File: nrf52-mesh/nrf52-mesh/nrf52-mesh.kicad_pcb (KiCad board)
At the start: 2 copper layers, 57.9 x 56.6 mm, 27 parts, among them J1 Conn_01x20_Male, J2 Conn_01x04_Male, J3 Conn_01x06_Male, U1 BL652

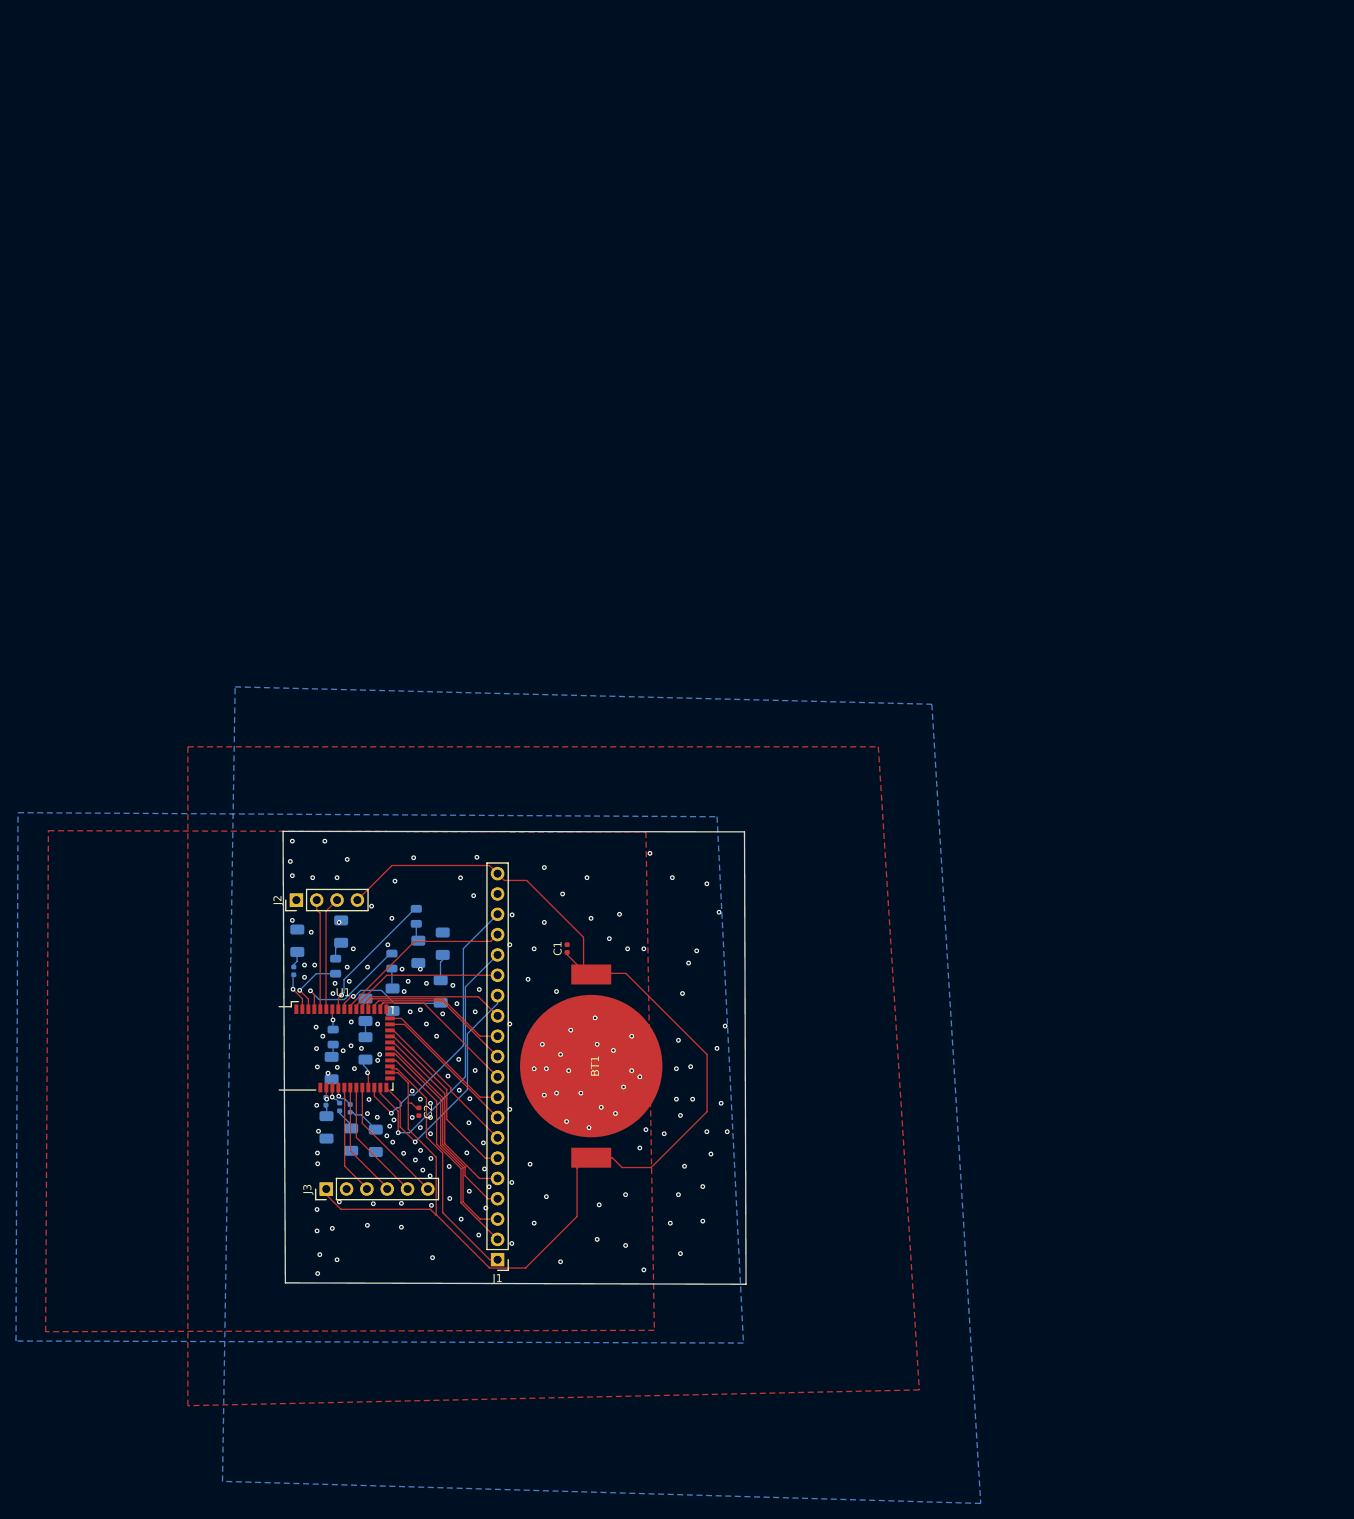
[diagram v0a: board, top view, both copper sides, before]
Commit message: CP2102N + MAX1555 + FAN5341 + TPS560200 + TLV62568
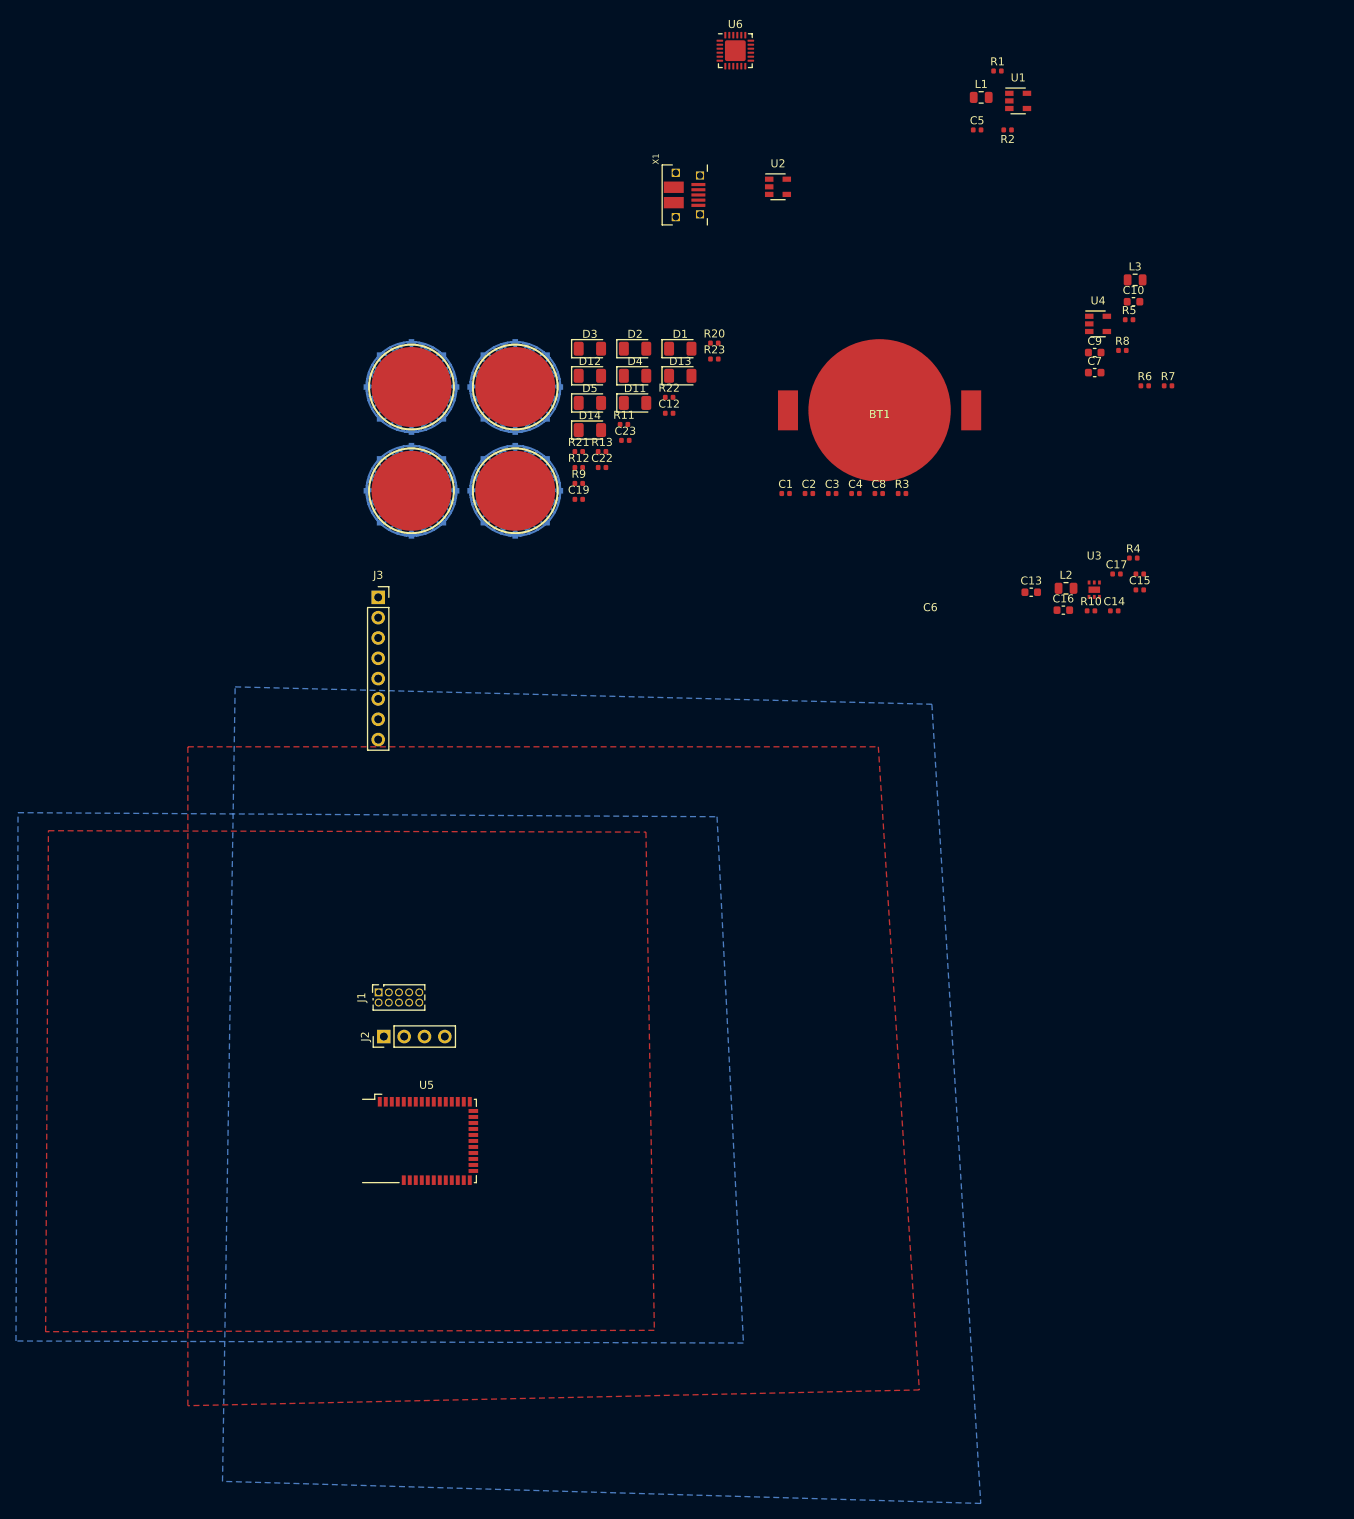
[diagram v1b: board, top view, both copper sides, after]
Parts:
- removed D10, D6, D7, D8, D9: LED, LED_SMD:LED_1206_3216Metric
- added C10: 10uF, Capacitor_SMD:C_0603_1608Metric, F.Cu at (288.0, -14.1)
- added C11: Cap, kifootp:CAPBUTTON, F.Cu at (197.8, -3.42)
- added C12: 100pF, Capacitor_SMD:C_0402_1005Metric, F.Cu at (230.0, -0.14)
- added C13: 10uF, Capacitor_SMD:C_0603_1608Metric, F.Cu at (275.2, 22.2)
- added C14: 1uF, Capacitor_SMD:C_0402_1005Metric, F.Cu at (285.6, 24.6)
- added C15: 1uF, Capacitor_SMD:C_0402_1005Metric, F.Cu at (288.8, 21.9)
- added C16: 10uF, Capacitor_SMD:C_0603_1608Metric, F.Cu at (279.3, 24.5)
- added C17: 0.1uF, Capacitor_SMD:C_0402_1005Metric, F.Cu at (285.9, 19.9)
- added C18: Cap, kifootp:CAPBUTTON, F.Cu at (210.7, 9.55)
- added C19: 100pF, Capacitor_SMD:C_0402_1005Metric, F.Cu at (218.7, 10.6)
- added C20: Cap, kifootp:CAPBUTTON, F.Cu at (210.7, -3.42)
- added C21: Cap, kifootp:CAPBUTTON, F.Cu at (197.8, 9.55)
- added C22: 100pF, Capacitor_SMD:C_0402_1005Metric, F.Cu at (221.6, 6.64)
- added C23: 100pF, Capacitor_SMD:C_0402_1005Metric, F.Cu at (224.5, 3.25)
- added C3: 0.1uF, Capacitor_SMD:C_0402_1005Metric, F.Cu at (250.4, 9.89)
- added C4: 1uF, Capacitor_SMD:C_0402_1005Metric, F.Cu at (253.3, 9.89)
- added C5: 4.7uF, Capacitor_SMD:C_0402_1005Metric, F.Cu at (268.5, -35.6)
- added C6: 10uF, Capacitor_SMD:C_0402_1005Metric, F.Cu at (288.8, 19.9)
- added C7: 10uF, Capacitor_SMD:C_0603_1608Metric, F.Cu at (283.2, -5.22)
- added C8: 0.1uF, Capacitor_SMD:C_0402_1005Metric, F.Cu at (256.2, 9.89)
- added C9: 10uF, Capacitor_SMD:C_0603_1608Metric, F.Cu at (283.2, -7.73)
- added D11: LED, LED_SMD:LED_1206_3216Metric, F.Cu at (225.7, -1.43)
- added D12: LED, LED_SMD:LED_1206_3216Metric, F.Cu at (220.1, -4.82)
- added D13: LED, LED_SMD:LED_1206_3216Metric, F.Cu at (231.4, -4.82)
- added D14: LED, LED_SMD:LED_1206_3216Metric, F.Cu at (220.1, 1.96)
- added L1: 2.2uH, Inductor_SMD:L_0805_2012Metric, F.Cu at (269.0, -39.6)
- added L2: 10uH, Inductor_SMD:L_0805_2012Metric, F.Cu at (279.6, 21.7)
- added L3: 10uH, Inductor_SMD:L_0805_2012Metric, F.Cu at (288.2, -16.8)
- added R11: 10kOhm, Resistor_SMD:R_0402_1005Metric, F.Cu at (224.3, 1.26)
- added R12: 10kOhm, Resistor_SMD:R_0402_1005Metric, F.Cu at (218.7, 6.64)
- added R13: 10kOhm, Resistor_SMD:R_0402_1005Metric, F.Cu at (221.6, 4.65)
- added R20: 10kOhm, Resistor_SMD:R_0402_1005Metric, F.Cu at (235.6, -8.91)
- added R21: 10kOhm, Resistor_SMD:R_0402_1005Metric, F.Cu at (218.7, 4.65)
- added R22: 10kOhm, Resistor_SMD:R_0402_1005Metric, F.Cu at (230.0, -2.13)
- added R23: 10kOhm, Resistor_SMD:R_0402_1005Metric, F.Cu at (235.6, -6.92)
- added U2: MAX1555, Package_TO_SOT_SMD:SOT-23-5, F.Cu at (243.6, -28.4)
- added U3: FAN5341, kifootp:FAN5341, F.Cu at (283.1, 21.9)
- added U4: TPS560200, Package_TO_SOT_SMD:SOT-23-5, F.Cu at (283.6, -11.3)
- added U5: BL652, RF_Module:Laird_BL652, F.Cu at (199.7, 90.8)
- added U6: CP2102N-A01-GQFN24, Package_DFN_QFN:QFN-24-1EP_4x4mm_P0.5mm_EP2.6x2.6mm, F.Cu at (238.3, -45.5)
- added X1: USBFCI_10103594, kifootp:FCI_10103594_MILL, F.Cu at (229.1, -27.4)
- C1: value 4.7uF -> 1uF
- C2: value 0.1uF -> 4.7uF
- D1, D2, D3, D4, D5: moved to F.Cu
- J1: value Conn_01x20_Male -> Conn_02x05_Odd_Even; footprint Connector_PinHeader_2.54mm:PinHeader_1x20_P2.54mm_Vertical -> Connector_PinSocket_1.27mm:PinSocket_2x05_P1.27mm_Vertical
- J3: value Conn_01x06_Male -> Conn_01x08; footprint Connector_PinHeader_2.54mm:PinHeader_1x06_P2.54mm_Vertical -> Connector_PinSocket_2.54mm:PinSocket_1x08_P2.54mm_Vertical
- R1: value R -> 450kOhm; moved to F.Cu
- R10: value R -> 1kOhm; footprint Resistor_SMD:R_1206_3216Metric -> Resistor_SMD:R_0402_1005Metric; moved to F.Cu
- R2, R3: value R -> 100kOhm; moved to F.Cu
- R4: value R -> 20 Ohm; moved to F.Cu
- R5: value R -> 200kOhm; footprint Resistor_SMD:R_0805_2012Metric -> Resistor_SMD:R_0402_1005Metric; moved to F.Cu
- R6: value R -> 100kOhm; footprint Resistor_SMD:R_0805_2012Metric -> Resistor_SMD:R_0402_1005Metric; moved to F.Cu
- R7: value R -> 105kOhm; footprint Resistor_SMD:R_0805_2012Metric -> Resistor_SMD:R_0402_1005Metric; moved to F.Cu
- R8: value R -> 20kOhm; footprint Resistor_SMD:R_0805_2012Metric -> Resistor_SMD:R_0402_1005Metric; moved to F.Cu
- R9: value R -> 10kOhm; footprint Resistor_SMD:R_1206_3216Metric -> Resistor_SMD:R_0402_1005Metric; moved to F.Cu
- U1: value BL652 -> TLV62568DBV; footprint RF_Module:Laird_BL652 -> Package_TO_SOT_SMD:SOT-23-5
- moved R1 152.8 mm to (271.0, -42.9), turned to 0 degrees
- moved R2 147.9 mm to (272.3, -35.6), turned to 180 degrees
- moved U1 145.4 mm to (273.6, -39.2)
- moved R7 132.4 mm to (292.3, -3.57), turned to 0 degrees
- moved R5 127.9 mm to (287.5, -11.8), turned to 0 degrees
- moved R6 118.4 mm to (289.4, -3.57), turned to 0 degrees
- moved R4 116.9 mm to (288.0, 18.0), turned to 0 degrees
- moved R8 113.1 mm to (286.6, -7.99), turned to 0 degrees
- moved D1 106.1 mm to (231.4, -8.21), turned to 0 degrees
- moved D2 105.0 mm to (225.7, -8.21), turned to 0 degrees
- moved R3 104.7 mm to (259.1, 9.89), turned to 0 degrees
- moved D3 102.7 mm to (220.1, -8.21), turned to 0 degrees
- moved R10 94.2 mm to (282.7, 24.6), turned to 0 degrees
- moved C2 91.4 mm to (247.5, 9.89), turned to 0 degrees
- moved BT1 89.5 mm to (256.3, -0.51), turned to 0 degrees
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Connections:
- C1 pad 1: +3V3 -> VUSB
- D1 pad 1: GND -> Net-(D1-Pad1)
- D1 pad 2: Net-(D1-Pad2) -> LEDIN
- D2 pad 1: GND -> Net-(D2-Pad1)
- D2 pad 2: Net-(D2-Pad2) -> Net-(D1-Pad1)
- D3 pad 1: GND -> Net-(D3-Pad1)
- D3 pad 2: Net-(D3-Pad2) -> Net-(D2-Pad1)
- D4 pad 1: GND -> Net-(D4-Pad1)
- D4 pad 2: Net-(D4-Pad2) -> Net-(D3-Pad1)
- D5 pad 1: GND -> LEDOUT
- D5 pad 2: Net-(D5-Pad2) -> Net-(D4-Pad1)
- J1 pad 2: Net-(J1-Pad2) -> SWDIO
- J1 pad 3: Net-(J1-Pad3) -> GND
- J1 pad 4: Net-(J1-Pad4) -> SWDCLK
- J1 pad 5: Net-(J1-Pad5) -> GND
- J1 pad 9: Net-(J1-Pad9) -> GND
- J2 pad 2: Net-(J2-Pad2) -> SWDIO
- J2 pad 3: Net-(J2-Pad3) -> SWDCLK
- J3 pad 3: Net-(J3-Pad3) -> io6
- J3 pad 4: Net-(J3-Pad4) -> io5
- J3 pad 5: Net-(J3-Pad5) -> io4
- J3 pad 6: Net-(J3-Pad6) -> io3
- R1 pad 1: Net-(D1-Pad2) -> +3V3
- R2 pad 1: Net-(D2-Pad2) -> Net-(R1-Pad2)
- R2 pad 2: Net-(R2-Pad2) -> GND
- R3 pad 1: Net-(D3-Pad2) -> +3V3
- R3 pad 2: Net-(R3-Pad2) -> CHARGE
- R4 pad 1: Net-(D4-Pad2) -> LEDOUT
- R4 pad 2: Net-(R4-Pad2) -> GND
- R5 pad 1: Net-(D5-Pad2) -> +15V
- R6 pad 1: Net-(D6-Pad2) -> Net-(R5-Pad2)
- R6 pad 2: Net-(R6-Pad2) -> GND
- R7 pad 1: Net-(D7-Pad2) -> +5V
- R8 pad 1: Net-(D8-Pad2) -> Net-(R7-Pad2)
- R8 pad 2: Net-(R8-Pad2) -> GND
- R9 pad 1: Net-(D9-Pad2) -> +3V3
- R9 pad 2: Net-(R9-Pad2) -> CAP1
- U1 pad 1: GND -> +5V
- U1 pad 2: Net-(R4-Pad2) -> GND
- U1 pad 3: Net-(R5-Pad2) -> Net-(L1-Pad2)
- U1 pad 4: Net-(R6-Pad2) -> +5V
- U1 pad 5: Net-(J2-Pad2) -> Net-(R1-Pad2)
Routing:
- net +3V3: track 154.1 -> 0.00 mm
- net Net-(J1-Pad18): track 35.0 -> 0.00 mm, vias 1 -> 0
- net Net-(J1-Pad16): track 34.7 -> 0.00 mm, vias 1 -> 0
- net Net-(J1-Pad14): track 30.8 -> 0.00 mm, vias 1 -> 0
- net Net-(J1-Pad1): track 30.7 -> 0.00 mm
- net Net-(J1-Pad2): track 28.4 -> 0.00 mm
- net Net-(J1-Pad3): track 27.9 -> 0.00 mm
- net Net-(J1-Pad4): track 25.3 -> 0.00 mm
- net Net-(J1-Pad5): track 24.2 -> 0.00 mm
- net Net-(J1-Pad17): track 22.7 -> 0.00 mm
- net Net-(J1-Pad6): track 22.0 -> 0.00 mm
- net Net-(J1-Pad15): track 19.7 -> 0.00 mm
- net Net-(J1-Pad7): track 19.3 -> 0.00 mm
- net Net-(J1-Pad12): track 19.2 -> 0.00 mm
- net Net-(J1-Pad11): track 19.1 -> 0.00 mm
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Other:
- board outline removed

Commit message: CP2102N + MAX1555 + FAN5341 + TPS560200 + TLV62568
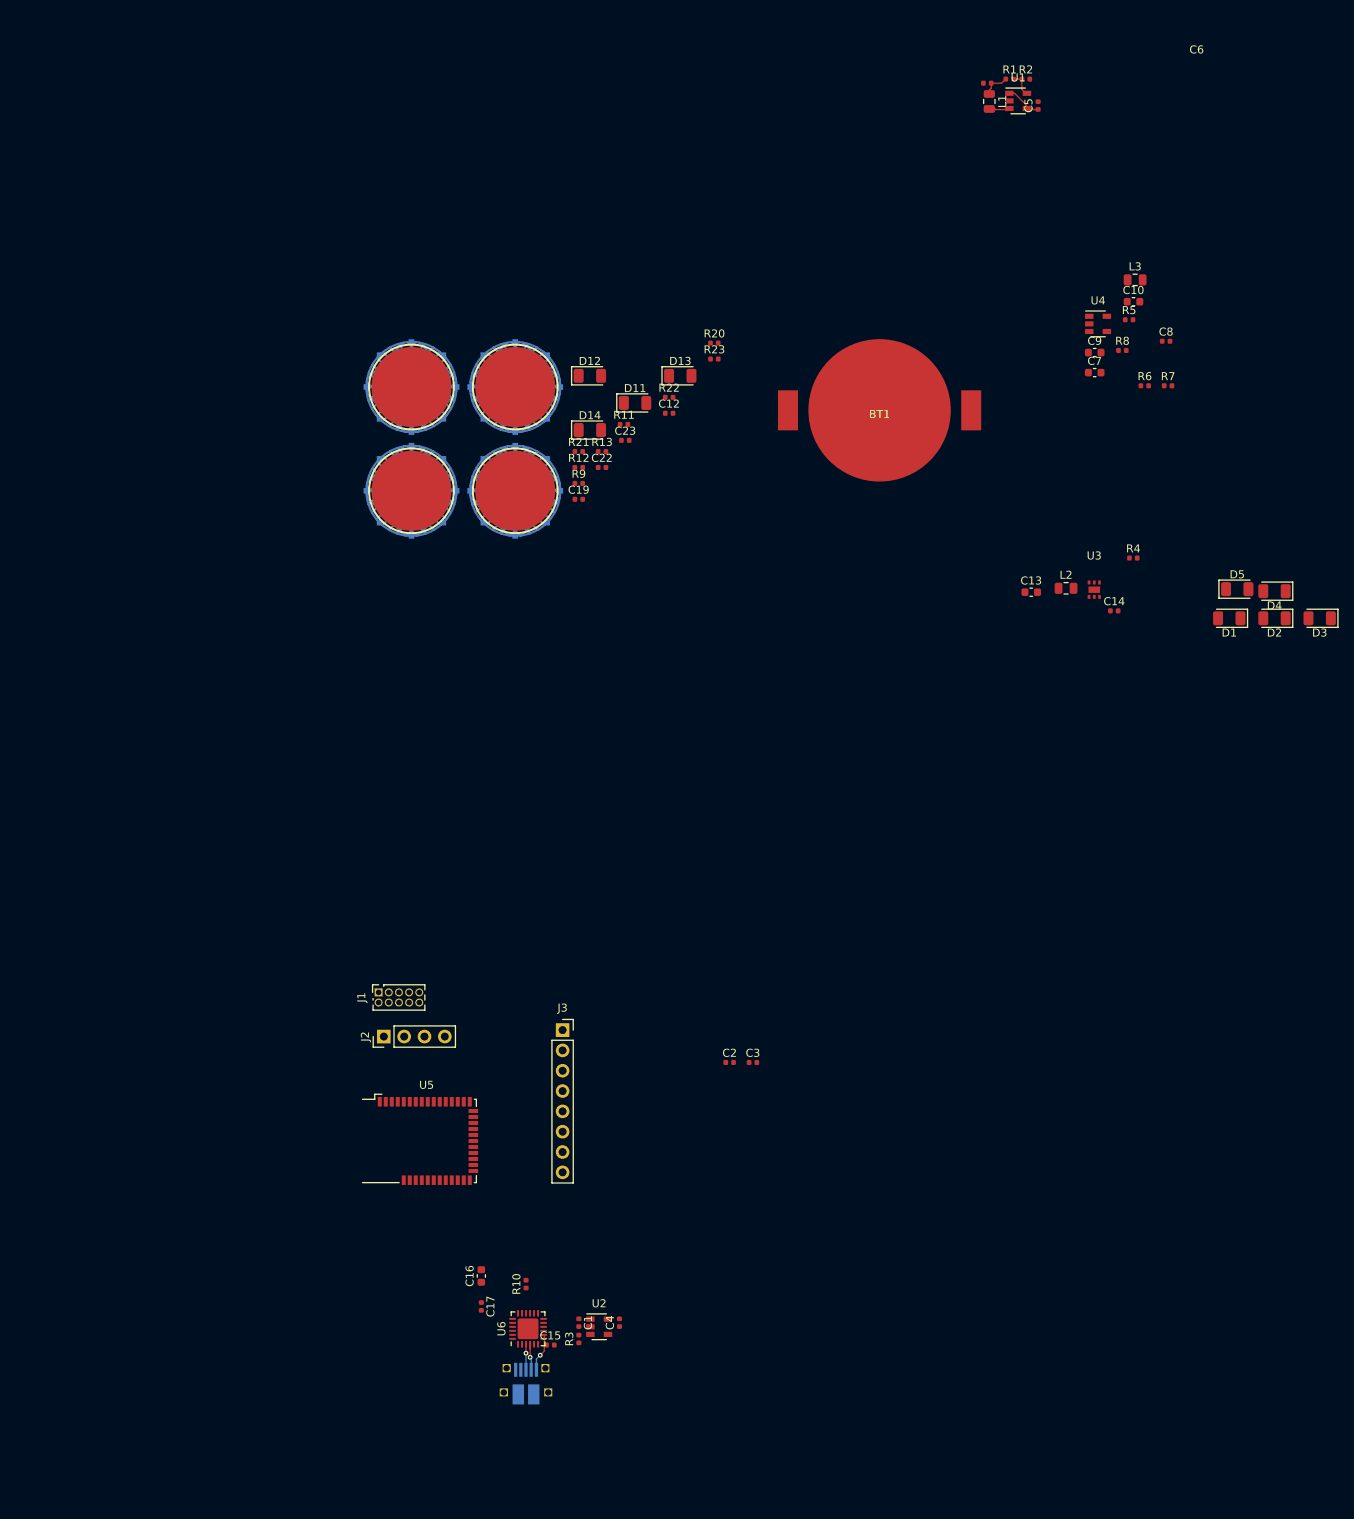
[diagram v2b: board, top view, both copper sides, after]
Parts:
- X1: moved to B.Cu
- moved U6 161.9 mm to (212.3, 114.3), turned to 90 degrees
- moved X1 152.3 mm to (212.1, 124.0), turned to 180 degrees
- moved U2 144.2 mm to (221.2, 114.0)
- moved C17 121.2 mm to (206.5, 111.5), turned to 270 degrees
- moved C15 119.7 mm to (215.1, 116.3)
- moved R3 113.1 mm to (218.7, 115.6), turned to 90 degrees
- moved C16 110.5 mm to (206.5, 107.7), turned to 90 degrees
- moved R10 109.9 mm to (212.1, 108.7), turned to 90 degrees
- moved C4 107.8 mm to (223.8, 113.5), turned to 90 degrees
- moved C1 106.8 mm to (218.7, 113.5), turned to 270 degrees
- moved D3 97.3 mm to (311.3, 25.5), turned to 180 degrees
- moved D2 86.7 mm to (305.6, 25.5), turned to 180 degrees
- moved D4 84.3 mm to (305.6, 22.1), turned to 180 degrees
- moved D5 84.2 mm to (301.0, 21.8)
- moved D1 76.5 mm to (300.0, 25.5), turned to 180 degrees
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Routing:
- net VUSB: track 0.00 -> 4.77 mm, vias 0 -> 1
- net +5V: track 0.00 -> 4.47 mm
- net Net-(U6-Pad4): track 0.00 -> 3.66 mm, vias 0 -> 1
- net +3V3: track 0.00 -> 3.44 mm
- net Net-(U6-Pad3): track 0.00 -> 3.35 mm, vias 0 -> 1
- net Net-(R1-Pad2): track 0.00 -> 3.03 mm
- net Net-(L1-Pad2): track 0.00 -> 2.57 mm
- removed copper zone on B.Cu, net GND
- removed copper zone on F.Cu, net GND
